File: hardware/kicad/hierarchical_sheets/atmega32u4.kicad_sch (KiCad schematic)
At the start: 19 parts, among them J1 0475900001, J3 TC2030, U1 ATmega32U4-A, Y2 16MHz

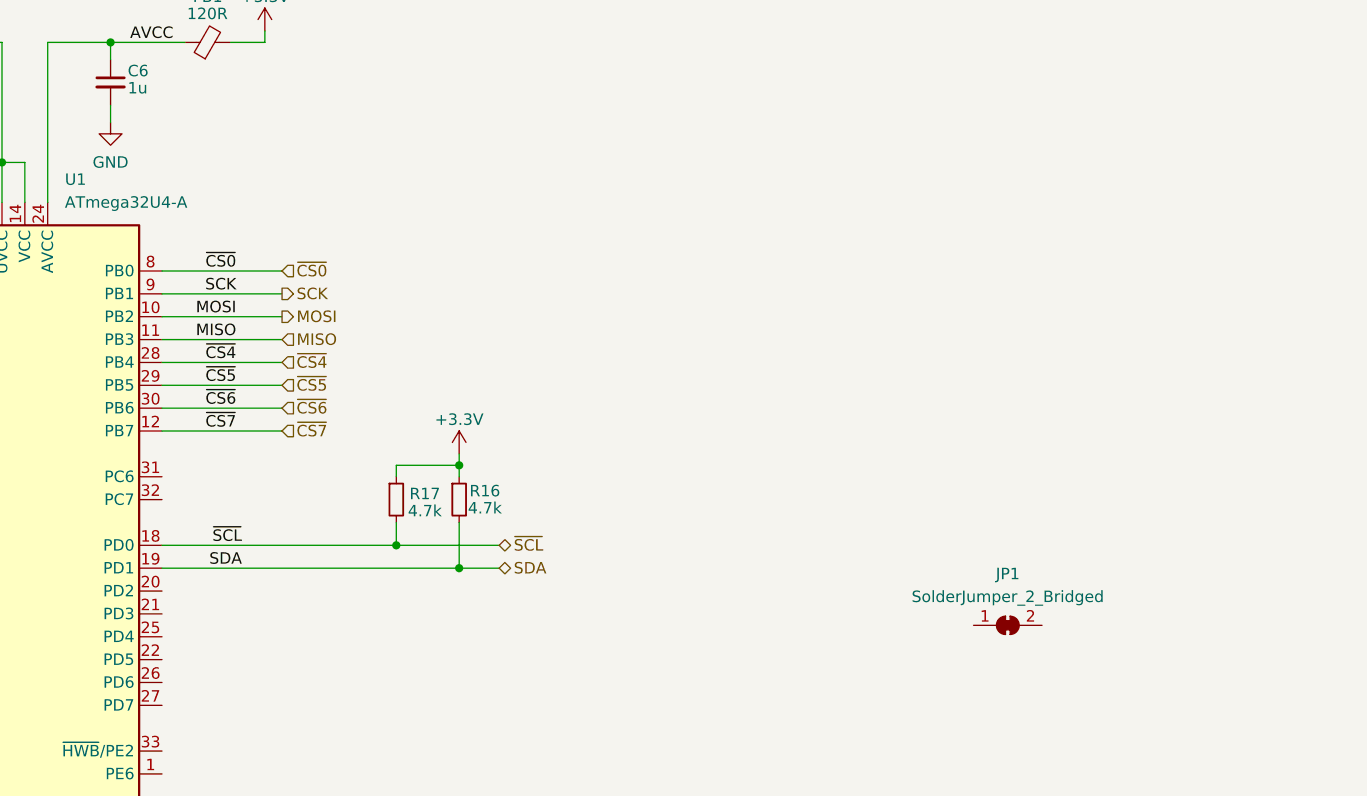
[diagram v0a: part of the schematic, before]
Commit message: added buzzer
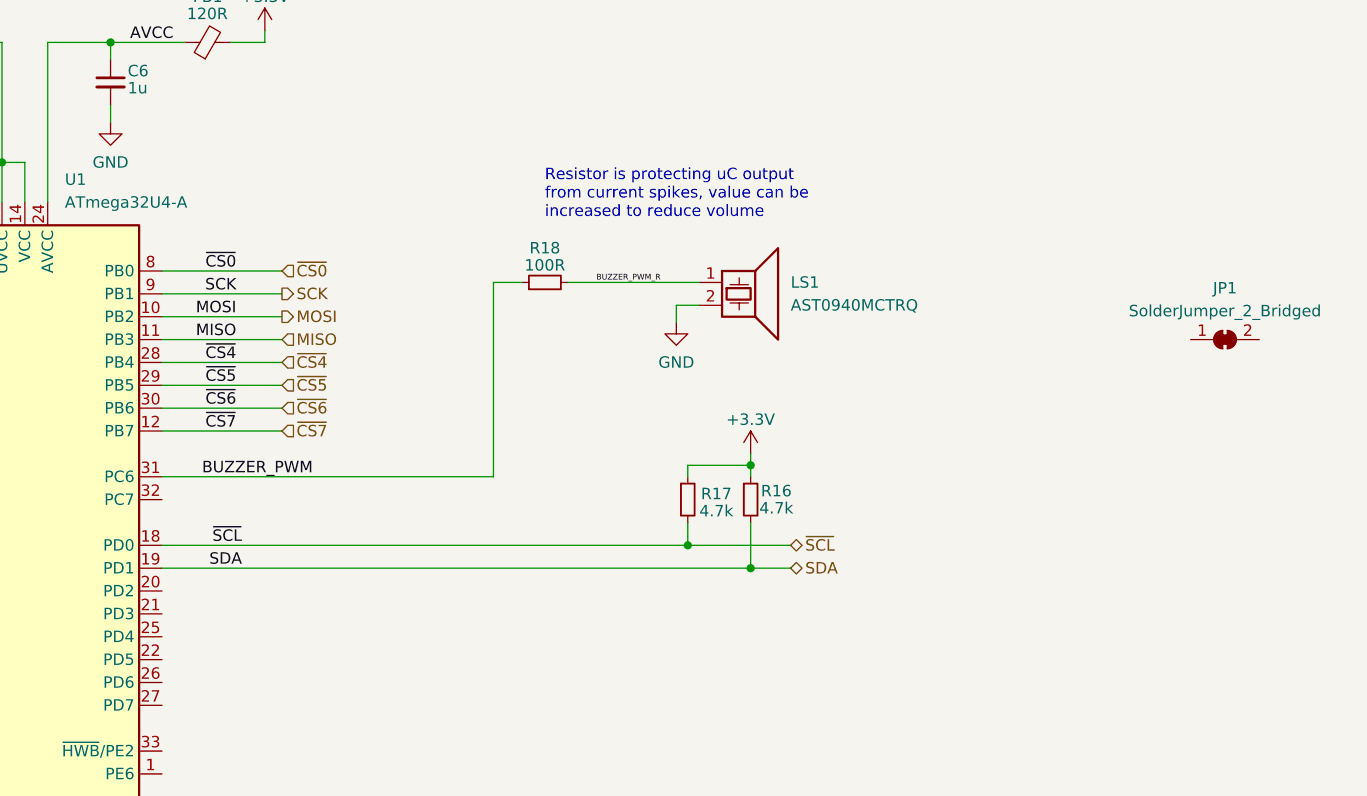
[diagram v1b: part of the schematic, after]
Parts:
- added LS1: AST0940MCTRQ, symbol Device:Speaker_Crystal
- added R18: 100R, symbol Device:R_Small
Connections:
- net GND: now also LS1.2
- net BUZZER_PWM: now reaches U1.31 (PC6)
- net BUZZER_PWM: now also R18.1
- new net BUZZER_PWM_R: LS1.1, R18.2
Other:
- note added: "Resistor is protecting uC output from current spikes, value can be increased to reduce volume"
- moved on the sheet: JP1, R16, R17

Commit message: massive comment upload
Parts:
- added D4: T3A53RGB, symbol Device:LED_RGBA
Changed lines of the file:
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@@
+    )
+  )
+  (symbol (lib_id "Device:LED_RGBA") (at 229.235 104.14 0) (unit 1)
+    (in_bom yes) (on_board yes) (dnp no) (fields_autoplaced)
+    (property "Reference" "D4" (at 229.235 91.44 0)
+      (effects (font (size 1.27 1.27)))
+    )
+    (property "Value" "T3A53RGB" (at 229.235 93.98 0)
+      (effects (font (size 1.27 1.27)))
+    )
+    (property "Footprint" "" (at 229.235 105.41 0)
+      (effects (font (size 1.27 1.27)) hide)
+    )
+    (property "Datasheet" "https://mm.digikey.com/Volume0/opasdata/d220001/medias/docus/4890/T3A53RGB-12C610111U1930.pdf" (at 229.235 105.41 0)
+      (effects (font (size 1.27 1.27)) hide)
+    )
+    (property "Digikey" "https://www.digikey.com/en/products/detail/harvatek-corporation/T3A53RGB-12C610111U1930/18997146" (at 229.235 104.14 0)
+      (effects (font (size 1.27 1.27)) hide)
+    )
+    (pin "1")
+    (pin "2")
+    (pin "3")
+    (pin "4")
+    (instances
+      (project "FC"
+        (path "/54cce219-8b98-4e71-96c4-f9ee784aa3bc/aac89dea-c005-40db-a234-32c8ed41f1e5"
+          (reference "D4") (unit 1)
+        )
+      )
     )
   )

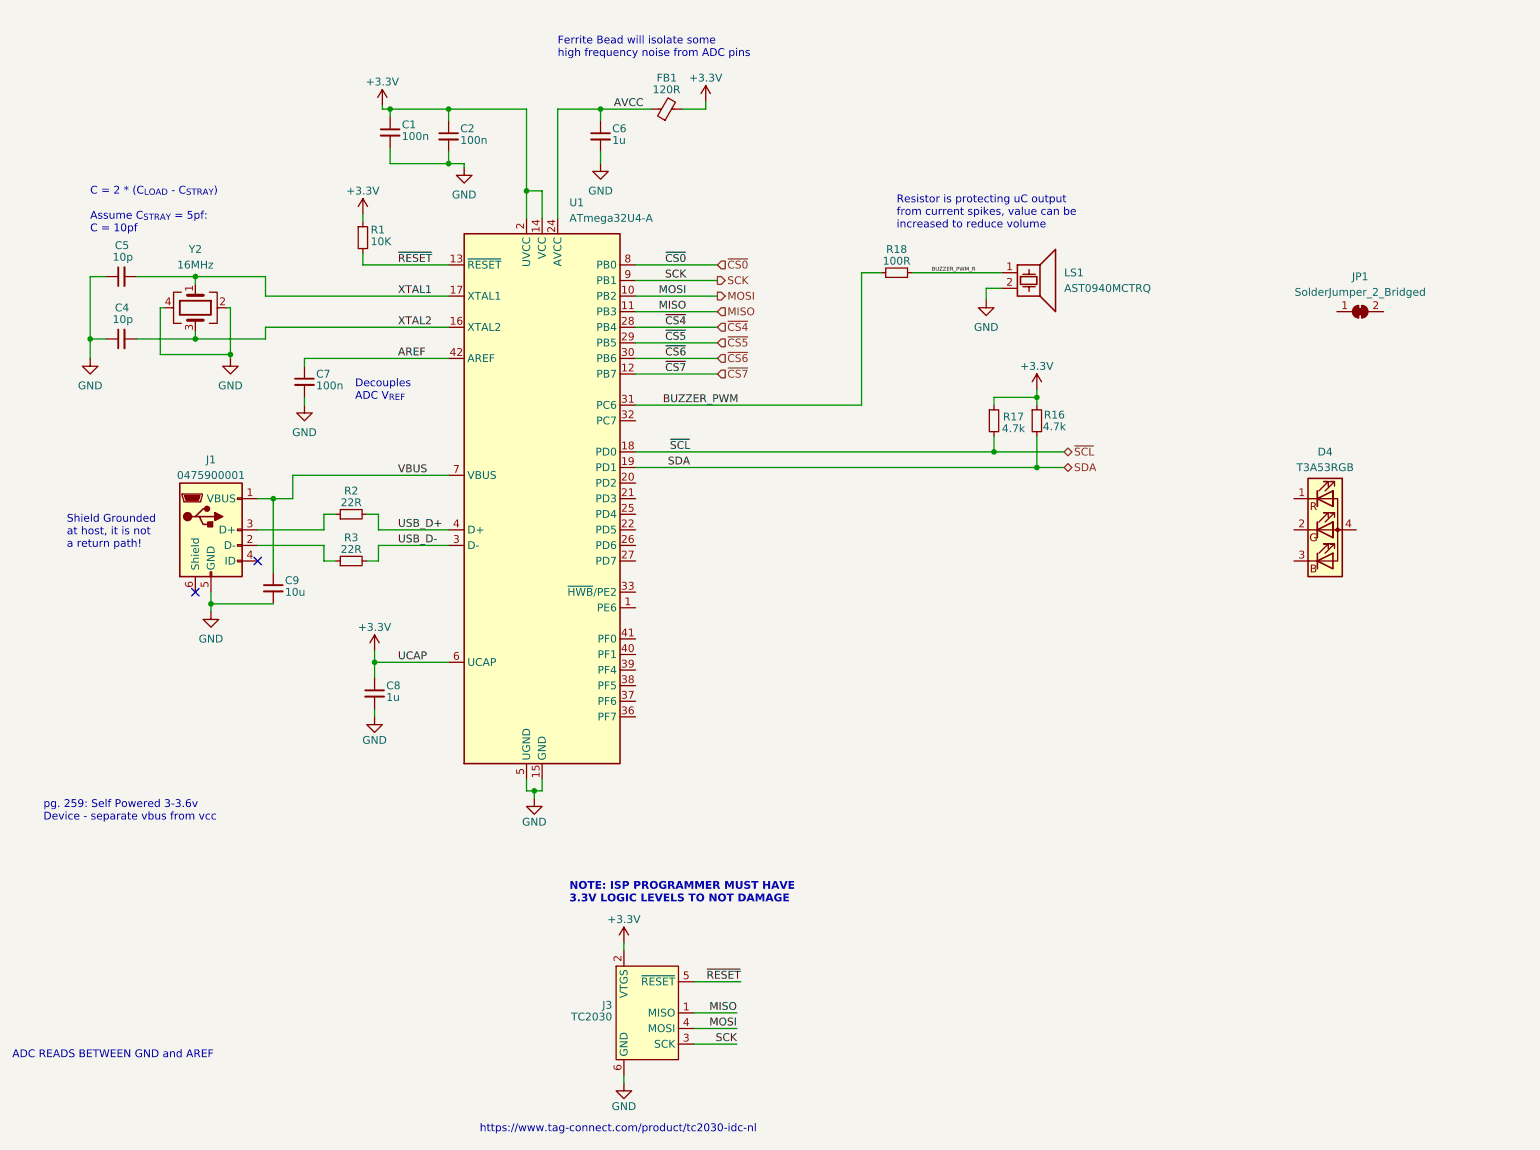
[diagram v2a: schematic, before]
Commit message: literally moved half the microcontroller pins :(
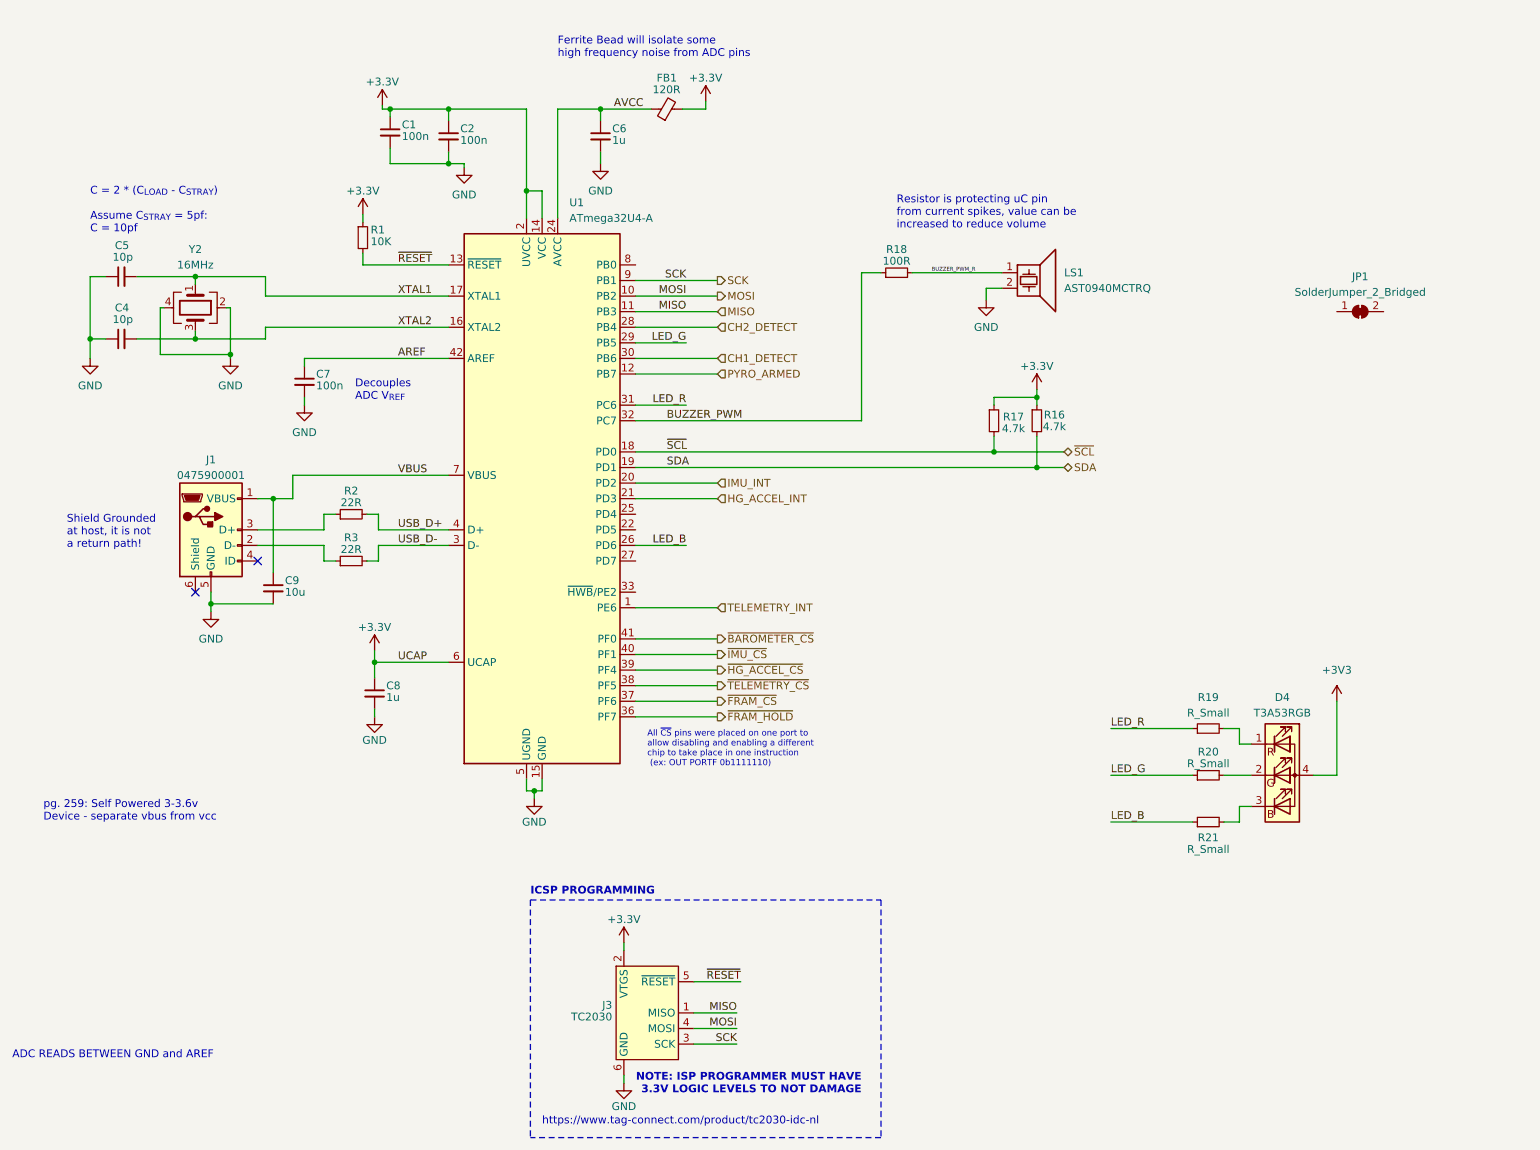
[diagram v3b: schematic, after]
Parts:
- added R19, R20, R21: R_Small, symbol Device:R_Small
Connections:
- net BUZZER_PWM: now also U1.32 (PC7); no longer U1.31 (PC6)
- net TELEMETRY_INT: now reaches U1.1 (PE6)
- net IMU_INT: now reaches U1.20 (PD2)
- net HG_ACCEL_INT: now reaches U1.21 (PD3)
- net LED_B: now reaches U1.26 (PD6)
- net LED_B: now also R21.1
- net ~{FRAM_HOLD}: now reaches U1.36 (PF7)
- net ~{FRAM_CS}: now reaches U1.37 (PF6)
- net ~{TELEMETRY_CS}: now reaches U1.38 (PF5)
- net ~{HG_ACCEL_CS}: now reaches U1.39 (PF4)
- net ~{IMU_CS}: now reaches U1.40 (PF1)
- net ~{BAROMETER_CS}: now reaches U1.41 (PF0)
- net at D4.1 (RK): now also R19.2
- net at D4.2 (GK): now also R20.2
- net at D4.3 (BK): now also R21.2
- net +3V3: now reaches D4.4 (A)
- net ~{CS0}: no longer names the net of U1.8 (PB0)
- net ~{CS4} renamed CH2_DETECT
- net ~{CS5} renamed LED_G
- net LED_G: now also R20.1
- net ~{CS6} renamed CH1_DETECT
- net ~{CS7} renamed PYRO_ARMED
- new net LED_R: R19.1, U1.31 (PC6)
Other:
- note added: "All ~{CS} pins were placed on one port to allow disabling and enabling a different chip to take place in one instruction (ex: OUT PORTF 0b1111110)"
- note added: "ICSP PROGRAMMING"
- note added: "Resistor is protecting uC pin from current spikes, value can be increased to reduce volume"
- note removed: "Resistor is protecting uC output from current spikes, value can be increased to reduce volume"
- moved on the sheet: D4

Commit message: microcontroller done?
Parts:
- removed JP1: SolderJumper_2_Bridged, symbol Jumper:SolderJumper_2_Bridged
- R19: value R_Small -> 100R
- R20, R21: value R_Small -> 68R
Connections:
- net LED_R_r: now reaches D4.1 (RK), R19.2
- net CH1_FIRE: now reaches U1.22 (PD5)
- net VBAT: now reaches U1.25 (PD4)
- net PYRO_CURRENT: now reaches U1.27 (PD7)
- net CH2_FIRE: now reaches U1.33 (~{HWB}/PE2)
- net LED_G_r: now reaches D4.2 (GK), R20.2
- net LED_B_r: now reaches D4.3 (BK), R21.2
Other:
- note added: "INDICATOR LED"
- note added: "NOTE: ICSP PROGRAMMER MUST HAVE 3.3V LOGIC LEVELS TO NOT DAMAGE"
- note added: "R: V_{f} = 2.0V - 2.3V G: V_{f} = 2.6V - 2.8V B: V_{f} = 2.7V - 3.0V Target: <10mA per LED, (V=IR -> R=V/I) RED: R = (3.3-2)/0.010, R = 130 -> ~100 Ω GREEN: R = (3.3-2.6)/0.010, R = 70 -> ~68 Ω BLUE: R = (3.3 - 2.7)/0.010, R = 60 -> ~68 Ω"
- note removed: "NOTE: ISP PROGRAMMER MUST HAVE 3.3V LOGIC LEVELS TO NOT DAMAGE"
- moved on the sheet: C1, C2, C4, C5, C6, C7, C8, C9, D4, FB1, J1, LS1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

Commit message: added ground station conversion breakout pads
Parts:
- added TP1, TP2, TP3, TP4, TP5, TP7, TP8, TP9: TestPoint, TestPoint:TestPoint_Pad_D1.5mm, symbol Connector:TestPoint
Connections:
- net CH1_DETECT: now also TP4.1
- net CH1_FIRE: now also TP7.1
- net CH2_DETECT: now also TP5.1
- net CH2_FIRE: now also TP8.1
- net IMU_INT: now also TP2.1
- net PYRO_CURRENT: now also TP1.1
- net TELEMETRY_INT: now also TP3.1
- net PB0: now reaches U1.8 (PB0)
- net PB0: now also TP9.1
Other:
- note added: "All ~{CS} pins were placed on one port to allow disabling and enabling a different chip to take place in one instruction (ex: OUT PORTF 0b1111110) -> enables barometer (ex: OUT PORTF 0b1111101) -> disables barometer and enables IMU"
- note added: "GROUND STATION CONVERSION"
- note removed: "All ~{CS} pins were placed on one port to allow disabling and enabling a different chip to take place in one instruction (ex: OUT PORTF 0b1111110)"

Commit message: full pin utilization
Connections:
- net CH2_FIRE: now also U1.8 (PB0); no longer U1.33 (~{HWB}/PE2)
- net PB0: no longer U1.8 (PB0)
- new net TELEMETRY_BUSY: U1.33 (~{HWB}/PE2)
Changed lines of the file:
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@@
     (stroke (width 0) (type default))
   )
-  (wire (pts (xy 112.395 57.785) (xy 125.73 57.785))
-    (stroke (width 0) (type default))
-  )
   (wire (pts (xy 61.595 106.045) (xy 63.5 106.045))
     (stroke (width 0) (type default))
@@
     (stroke (width 0) (type default))
   )
-  (wire (pts (xy 112.395 111.125) (xy 125.73 111.125))
+  (wire (pts (xy 112.395 57.785) (xy 125.73 57.785))
     (stroke (width 0) (type default))
   )
@@
     (stroke (width 0) (type default))
   )
+  (wire (pts (xy 112.395 111.125) (xy 125.73 111.125))
+    (stroke (width 0) (type default))
+  )
   (wire (pts (xy 84.455 41.275) (xy 81.915 41.275))
     (stroke (width 0) (type default))
@@
     (effects (font (size 1.27 1.27)) (justify left bottom))
   )
-  (label "CH2_FIRE" (at 114.935 111.125 0) (fields_autoplaced)
+  (label "CH2_FIRE" (at 114.935 57.785 0) (fields_autoplaced)
     (effects (font (size 0.63 0.63)) (justify left bottom))
   )
@@
     (effects (font (size 1.27 1.27)) (justify left bottom))
   )
+  (label "TELEMETRY_BUSY" (at 114.935 111.125 0) (fields_autoplaced)
+    (effects (font (size 0.63 0.63)) (justify left bottom))
+  )
   (label "LED_B" (at 120.65 103.505 180) (fields_autoplaced)
     (effects (font (size 1.27 1.27)) (justify right bottom))
@@
     (effects (font (size 0.63 0.63)) (justify left bottom))
   )
-  (label "PB0" (at 125.73 57.785 180) (fields_autoplaced)
-    (effects (font (size 1.27 1.27)) (justify right bottom))
-  )
   (label "PYRO_CURRENT" (at 114.935 106.045 0) (fields_autoplaced)
     (effects (font (size 0.63 0.63)) (justify left bottom))
@@
     (effects (font (size 1.27 1.27)) (justify left))
   )
+  (hierarchical_label "TELEMETRY_BUSY" (shape input) (at 125.73 111.125 0) (fields_autoplaced)
+    (effects (font (size 1.27 1.27)) (justify left))
+  )
   (hierarchical_label "~{HG_ACCEL_CS}" (shape output) (at 125.73 123.825 0) (fields_autoplaced)
     (effects (font (size 1.27 1.27)) (justify left))
@@
     (effects (font (size 1.27 1.27)) (justify left))
   )
-  (hierarchical_label "CH2_FIRE" (shape output) (at 125.73 111.125 0) (fields_autoplaced)
+  (hierarchical_label "CH2_FIRE" (shape output) (at 125.73 57.785 0) (fields_autoplaced)
     (effects (font (size 1.27 1.27)) (justify left))
   )

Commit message: file sync
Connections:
- net HG_ACCEL_INT: now also TP3.1
- net TELEMETRY_INT: no longer TP3.1
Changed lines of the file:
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@@
     (effects (font (size 1.27 1.27)) (justify right bottom))
   )
-  (label "TELEMETRY_INT" (at 209.55 46.355 0) (fields_autoplaced)
+  (label "HG_ACCEL_INT" (at 209.55 46.355 0) (fields_autoplaced)
     (effects (font (size 1.27 1.27)) (justify left bottom))
   )
@@
     (effects (font (size 0.63 0.63)) (justify left bottom))
   )
+  (label "HG_ACCEL_INT" (at 114.935 95.885 0) (fields_autoplaced)
+    (effects (font (size 0.63 0.63)) (justify left bottom))
+  )

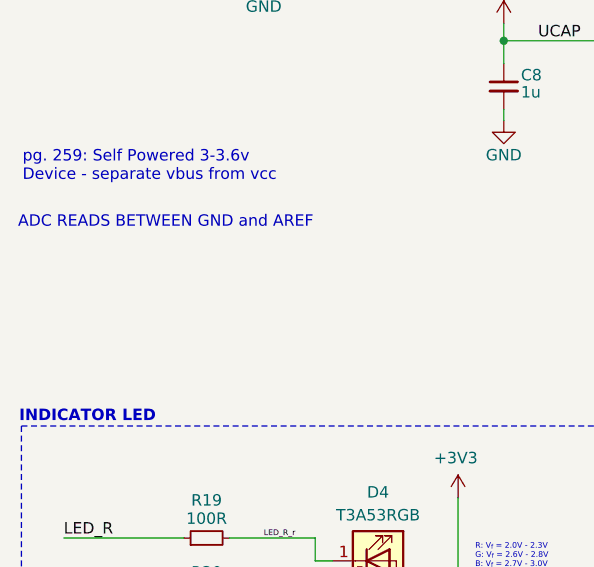
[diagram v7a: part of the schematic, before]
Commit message: added max current
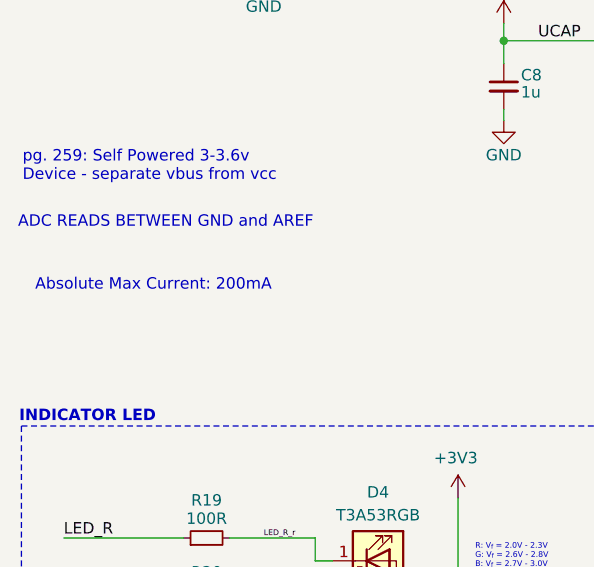
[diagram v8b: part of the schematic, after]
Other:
- note added: "Absolute Max Current: 200mA"
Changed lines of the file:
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@@
+    (effects (font (size 1.27 1.27)) (justify left bottom))
+  )
+  (text "Absolute Max Current: 200mA" (at 17.78 150.495 0)
     (effects (font (size 1.27 1.27)) (justify left bottom))
   )
